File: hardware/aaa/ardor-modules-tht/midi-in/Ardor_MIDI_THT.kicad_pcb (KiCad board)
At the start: 2 copper layers, 85 x 70 mm, 20 parts, among them J101 POWER INPUT + UART OUTPUT TO 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, J202 MIDI INPUT FROM DIN SOCKET, J203 METAL CASE BOND + GROUND, U201 onsemi H11L1M

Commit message: fix(hardware): use Hestore TVS diodes in hand-assembly modules
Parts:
- D202: value SA5.0CA-E3/54 -> 1.5KE6.8CA; footprint Diode_THT:D_DO-15_P10.16mm_Horizontal -> Ardor_THT:D_TVS_DC_1.5KE_P15.24mm
- moved D202 2.54 mm to (56.0, 72.6)
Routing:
- net Net-(D201-K): track 31.8 -> 37.7 mm
- net /MIDI_5: track 70.0 -> 73.7 mm
- net Net-(R202-Pad2): track 30.0 -> 28.0 mm
- net /CHASSIS: track 135.3 -> 134.2 mm
- net Net-(D201-A): track 34.2 -> 35.2 mm
- net /+3V3: track 44.6 -> 45.1 mm

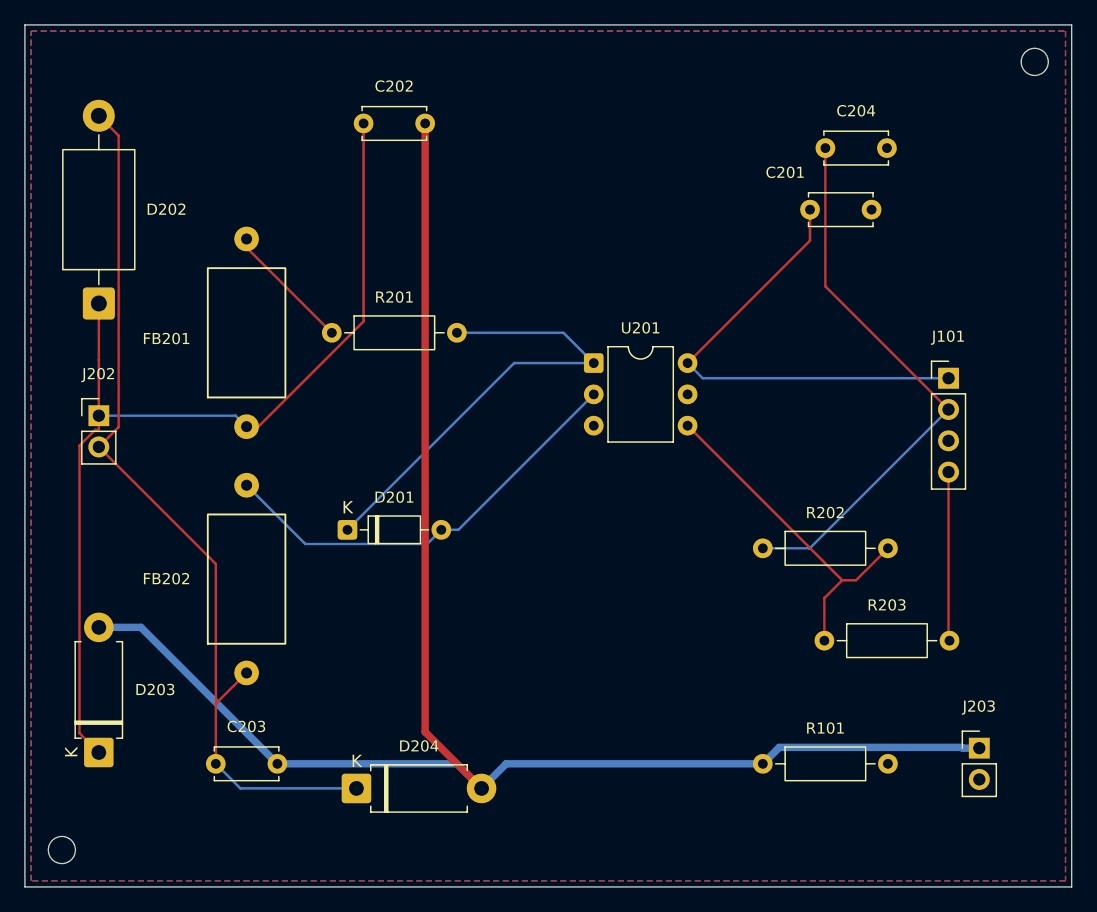
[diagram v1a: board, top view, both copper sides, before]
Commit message: feat(hardware): compact layouts and adopt Hestore module packages
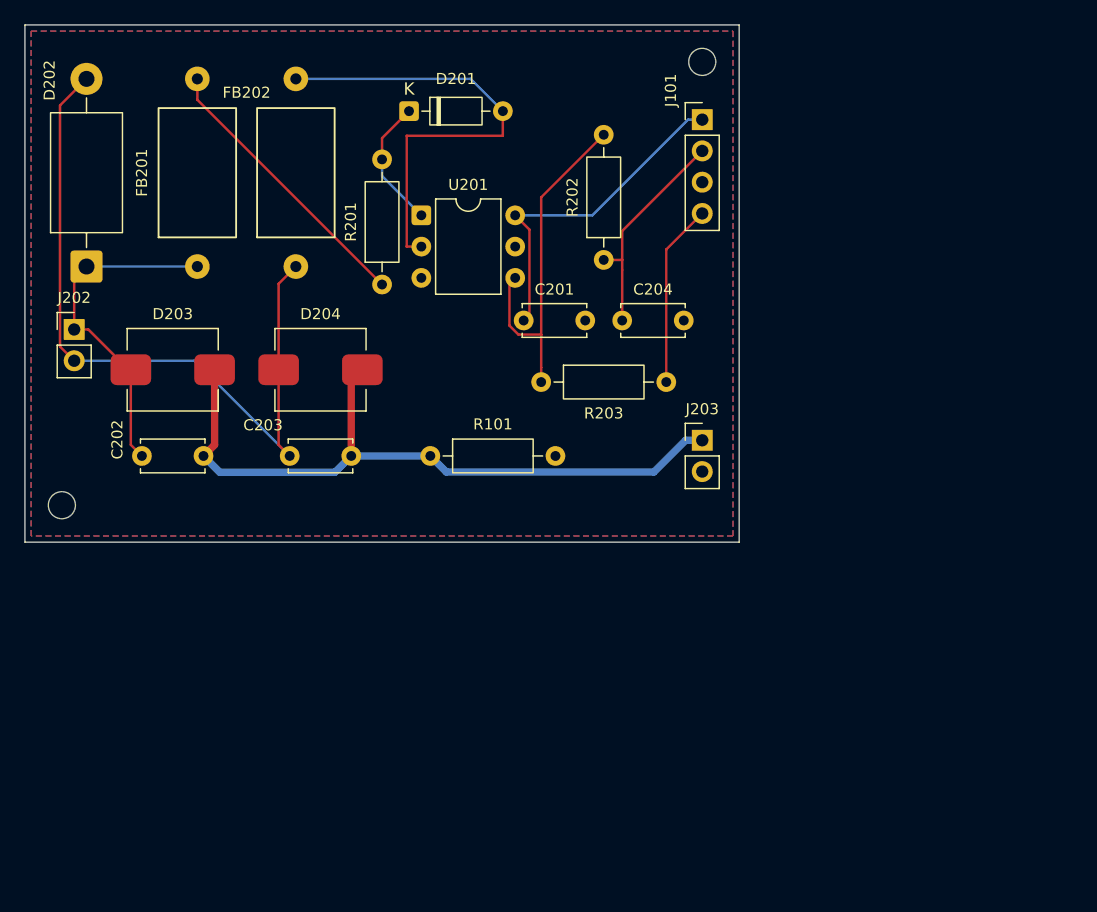
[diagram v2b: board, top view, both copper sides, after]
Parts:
- D203, D204: value SA24CA-E3/54 -> SMDJ24CA; footprint Diode_THT:D_DO-15_P10.16mm_Horizontal -> Ardor_THT:D_SMC_Bidirectional_Handsolder
- moved R101 36.8 mm to (82.9, 85.0)
- moved D201 34.4 mm to (81.2, 57.0)
- moved D204 34.1 mm to (74.0, 78.0)
- moved J203 33.6 mm to (105.0, 83.7)
- moved FB202 33.2 mm to (72.0, 69.6)
- moved C202 32.4 mm to (59.5, 85.0)
- moved D203 31.7 mm to (62.0, 78.0), turned to 0 degrees
- moved R203 31.1 mm to (91.9, 79.0)
- moved J101 29.0 mm to (105.0, 57.7)
- moved H1 28.0 mm to (53.0, 89.0)
- moved H2 27.0 mm to (105.0, 53.0)
- moved R202 26.7 mm to (97.0, 69.1), turned to 90 degrees
- moved C203 25.7 mm to (71.5, 85.0)
- moved C201 24.9 mm to (90.5, 74.0)
- moved C204 21.6 mm to (98.5, 74.0)
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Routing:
- net /CHASSIS: track 134.2 -> 58.0 mm
- net /MIDI_4: track 79.4 -> 27.9 mm
- net /+3V3: track 45.1 -> 18.0 mm
- net Net-(D201-K): track 37.7 -> 10.7 mm
- net Net-(FB201-Pad2): track 10.5 -> 22.9 mm
- net /MIDI_5: track 73.7 -> 61.3 mm
- net /+5V: track 38.3 -> 27.6 mm
- net Net-(D201-A): track 35.2 -> 37.9 mm
- net Net-(J101-Pin_4): track 13.7 -> 14.9 mm
- net Net-(R202-Pad2): track 28.0 -> 29.1 mm
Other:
- board size 85 x 70 mm -> 58 x 42 mm
